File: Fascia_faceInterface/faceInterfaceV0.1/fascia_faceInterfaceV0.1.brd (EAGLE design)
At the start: 200 x 123.7 mm, 16 parts, among them J1 MOLEX_52437-247_FLEX, J2 SM04B-SRSS-TB(LF)(SN)

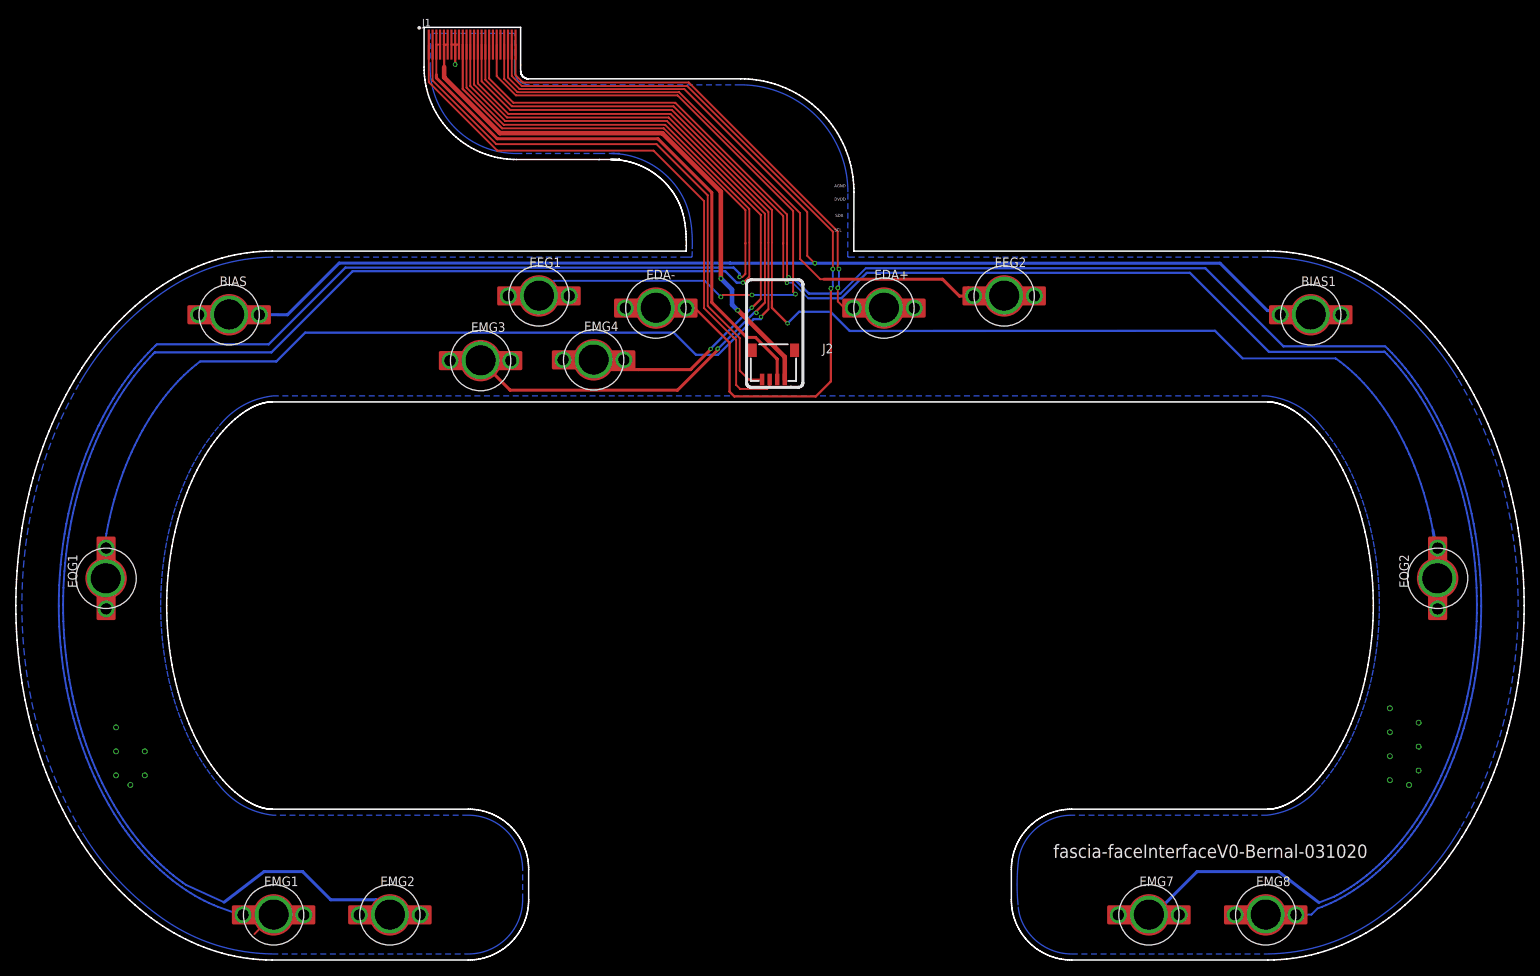
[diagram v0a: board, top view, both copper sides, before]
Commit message: Fixes for the faceinterface issue
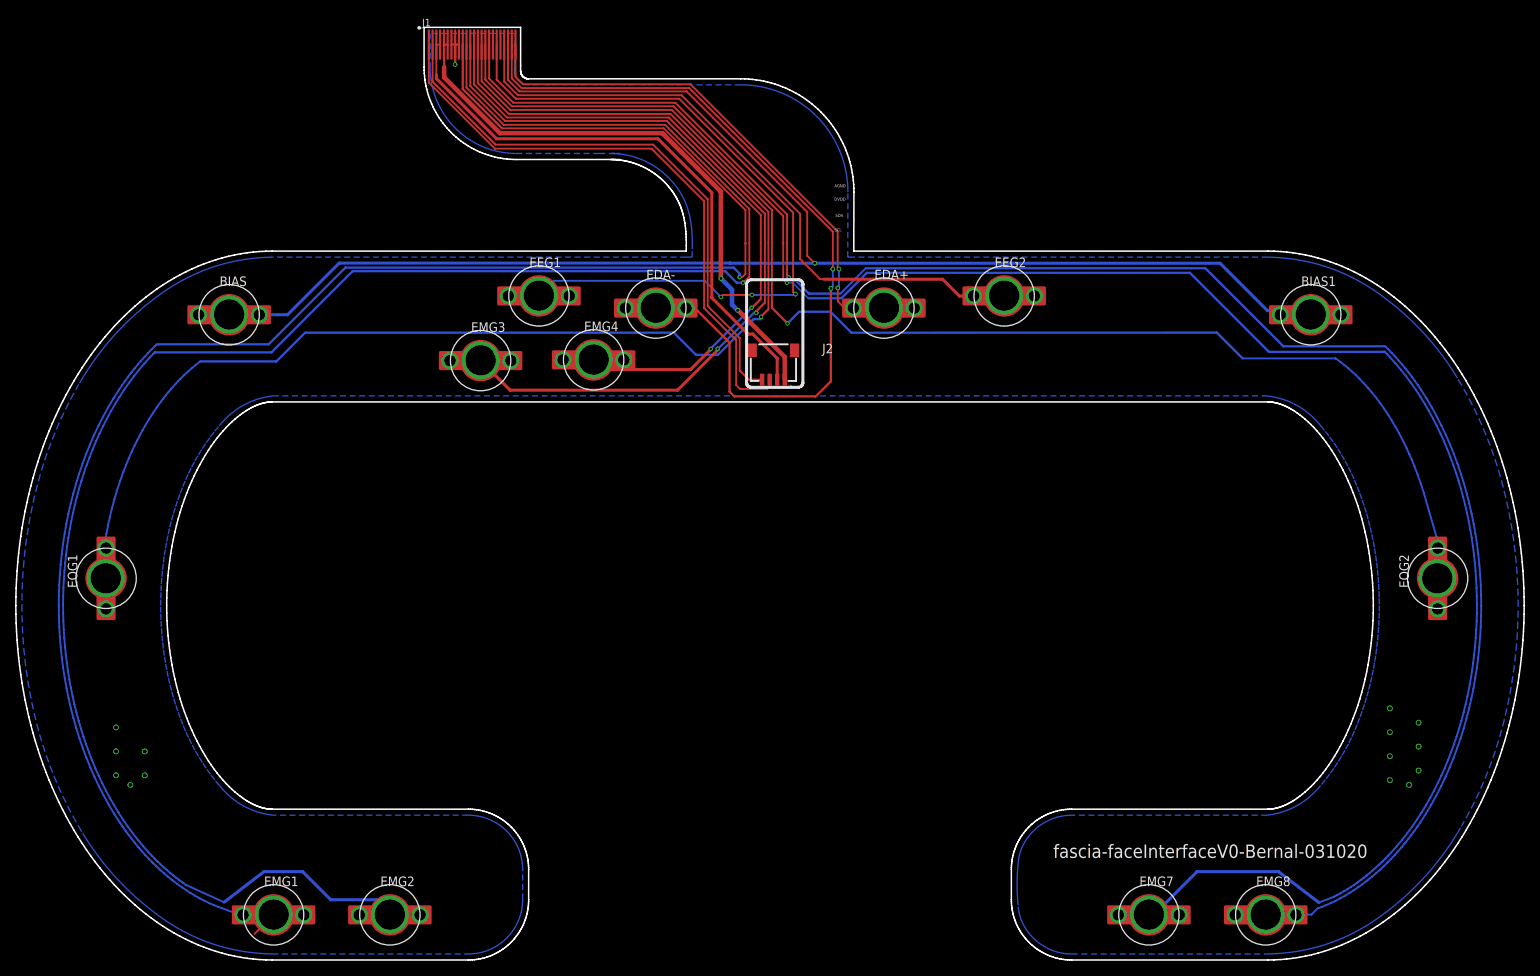
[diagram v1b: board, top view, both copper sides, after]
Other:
- outline, holes or cut-outs redrawn
